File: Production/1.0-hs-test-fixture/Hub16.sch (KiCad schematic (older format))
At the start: 83 parts, among them J1 USB_C_Receptacle_USB2.0, J2 AVR-ISP-6, J3 AVR-ISP-6, J4 AVR-ISP-6, J5 Conn_01x02_Male, K1 Kailh Hotswap Socket, K11 Kailh Hotswap Socket, K12 Kailh Hotswap Socket, K13 Kailh Hotswap Socket, K14 Kailh Hotswap Socket, K16 Kailh Hotswap Socket, K17 Kailh Hotswap Socket, K18 Kailh Hotswap Socket, K19 Kailh Hotswap Socket, K2 Kailh Hotswap Socket, K3 Kailh Hotswap Socket, K4 Kailh Hotswap Socket, K6 Kailh Hotswap Socket, K7 Kailh Hotswap Socket, K8 Kailh Hotswap Socket, K9 Kailh Hotswap Socket, Q1 BSS138, Q10 BSS138, Q11 BSS138, Q12 BSS138, Q13 BSS138, Q14 BSS138, Q15 BSS138, Q16 BSS138, Q2 BSS138, Q3 BSS138, Q4 BSS138, Q5 BSS138, Q6 BSS138, Q7 BSS138, Q8 BSS138, Q9 BSS138, SW1 EVQPUL, SW2 EC11 Encoder, SW3 EC11 Encoder, U1 74HC595, U2 ATMEGA32U4, U3 74HC595, Y1 16MHz

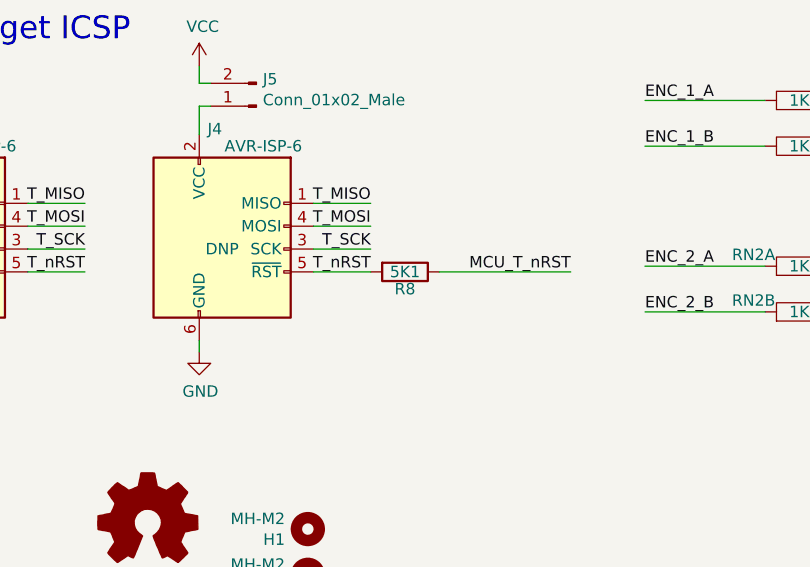
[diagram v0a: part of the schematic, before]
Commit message: update bare-bones spelling + text fixture update
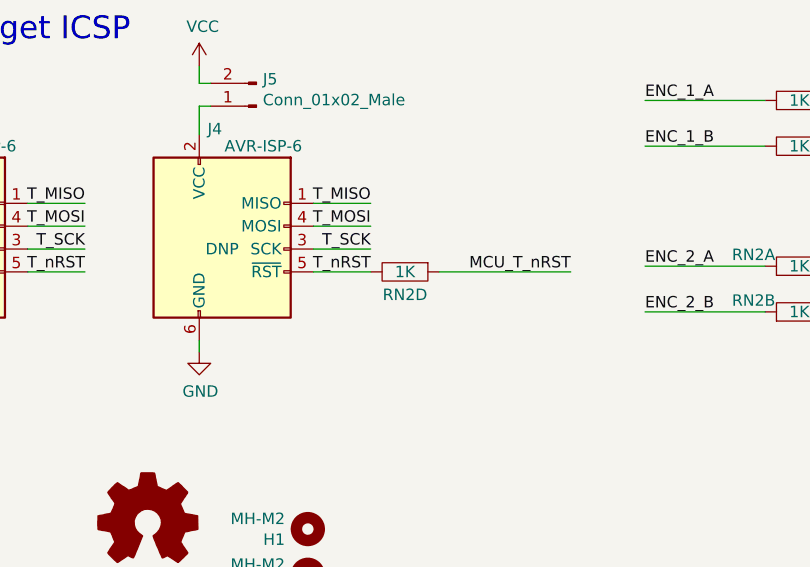
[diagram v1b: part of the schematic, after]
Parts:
- removed R8: 5K1, Resistor_SMD:R_0603_1608Metric, symbol Device:R
- added unit 4 of RN2
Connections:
- net MCU_T_nRST: now also RN2.1
- net T_nRST: now also RN2.8
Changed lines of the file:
@@
 Wire Wire Line
 	6600 3575 7125 3575
-$Comp
-L Device:R R?
-U 1 1 6031E633
-P 7275 5950
-AR Path="/5E5406D9/6031E633" Ref="R?"  Part="1"
-AR Path="/6031E633" Ref="R8"  Part="1"
-F 0 "R8" V 7350 5950 50  0000 C CNN
-F 1 "5K1" V 7275 5950 50  0000 C CNN
-F 2 "Resistor_SMD:R_0603_1608Metric" V 7205 5950 50  0001 C CNN
-F 3 "~" H 7275 5950 50  0001 C CNN
-F 4 "118-CR0603-JW-512ELFCT-ND " H 7275 5950 50  0001 C CNN "DigiKey"
-F 5 "CR0603-JW-512ELF " H 7275 5950 50  0001 C CNN "MPN"
-F 6 "Y  - Same spec" H 7275 5950 50  0001 C CNN "Substitue Allowed?"
-F 7 "C14677" H 7275 5950 50  0001 C CNN "LCSC"
-F 8 "Bourns" H 7275 5950 50  0001 C CNN "Manufacturer"
-F 9 "LCSC: Substitute PN" H 7275 5950 50  0001 C CNN "Notes"
-	1    7275 5950
-	0    1    1    0
-$EndComp
 Text Label 8000 5950 2    50   ~ 0
 MCU_T_nRST
@@
 	-1   0    0    1
 $EndComp
+$Comp
+L josh-passive:RN RN2
+U 4 1 5FBF5549
+P 7275 5950
+F 0 "RN2" H 7275 6050 50  0000 C CNN
+F 1 "1K" H 7275 5950 50  0000 C CNN
+F 2 "Resistor_SMD:R_Array_Convex_4x0603" V 7275 5950 50  0001 C CNN
+F 3 "~" V 7275 5950 50  0001 C CNN
+	4    7275 5950
+	-1   0    0    1
+$EndComp

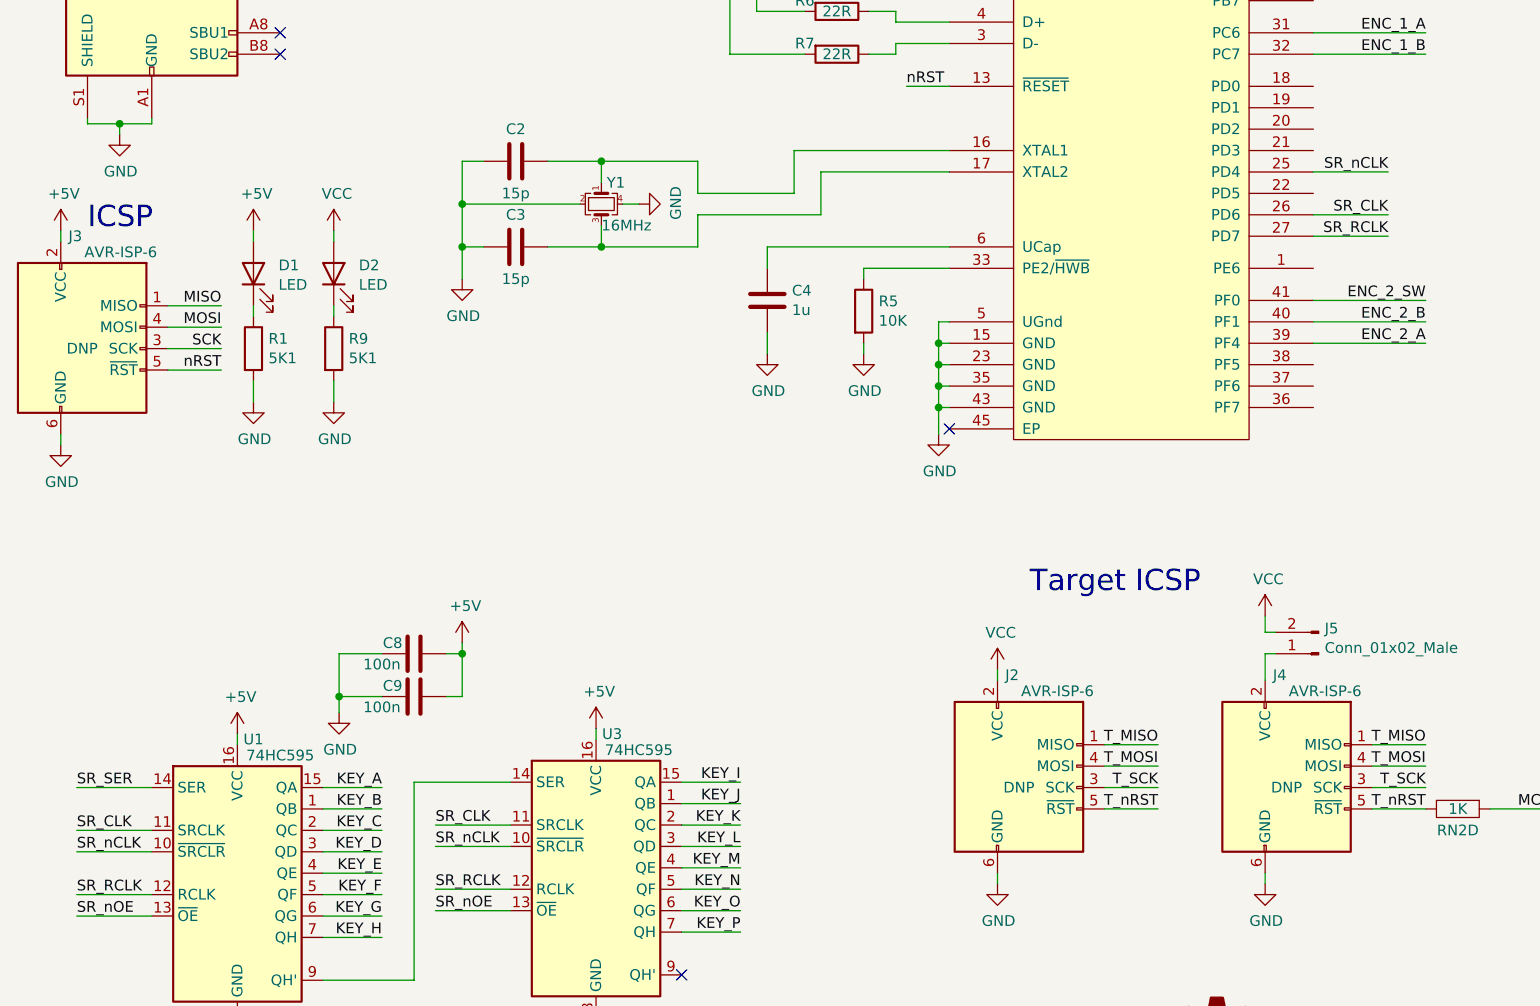
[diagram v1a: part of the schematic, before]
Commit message: test fixture for keys working
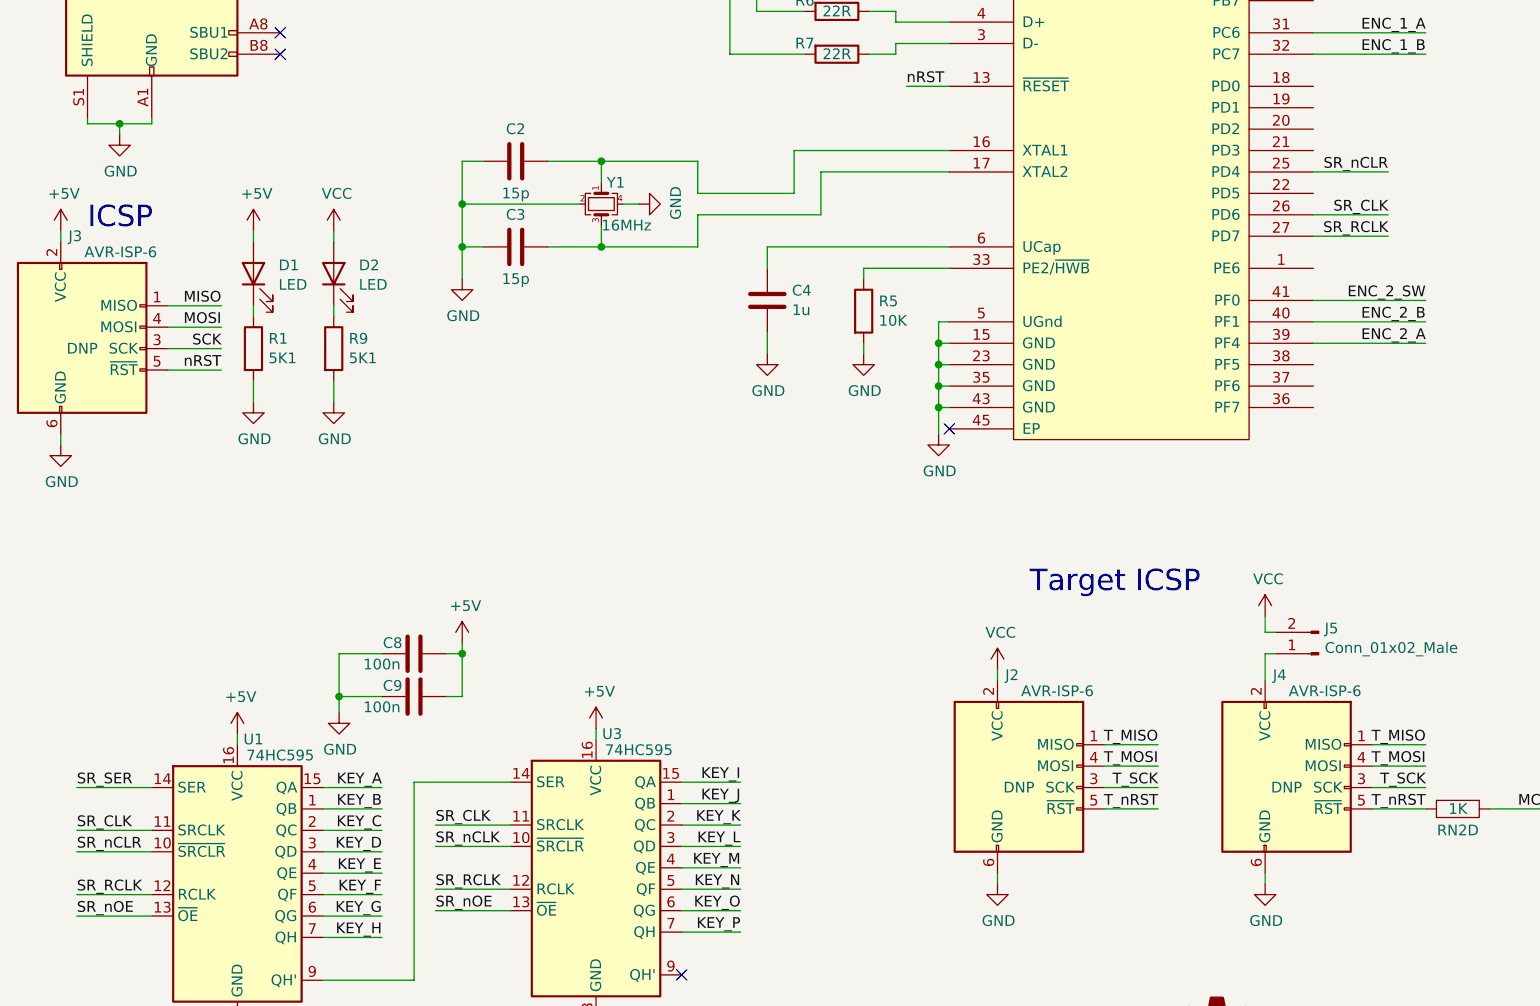
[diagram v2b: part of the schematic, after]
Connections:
- net SR_nCLK: no longer U1.10 (~SRCLR), U2.25 (PD4)
- new net SR_nCLR: U1.10 (~SRCLR), U2.25 (PD4)
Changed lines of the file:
@@
 	825  6450 1175 6450
 Text Label 825  6150 0    50   ~ 0
-SR_nCLK
+SR_nCLR
 Wire Wire Line
 	825  6150 1175 6150
@@
 	6950 1875 6600 1875
 Text Label 6950 2975 2    50   ~ 0
-SR_nCLK
+SR_nCLR
 Wire Wire Line
 	6950 2975 6600 2975
